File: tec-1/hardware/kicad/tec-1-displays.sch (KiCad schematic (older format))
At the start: 67 parts, among them J2 Conn_01x02, J3 LCD, Q1 2N3904, Q10 AO3400A, Q11 AO3400A, Q12 AO3400A, Q13 AO3400A, Q14 AO3400A, Q15 AO3400A, Q16 AO3400A, Q17 AO3400A, Q18 AO3400A, Q19 AO3400A, Q2 AO3400A, Q20 AO3400A, Q21 AO3400A, Q22 AO3400A, Q23 AO3400A, Q3 AO3400A, Q4 AO3400A, Q5 AO3400A, Q6 AO3400A, Q7 AO3400A, Q8 AO3400A, Q9 AO3400A, U10 74HCT574, U11 74HCT574, U12 LED_SEGMENT_CC_x2, U13 LED_SEGMENT_CC_x4, U14 74HCT574, U15 74HCT574, U16 74HCT574

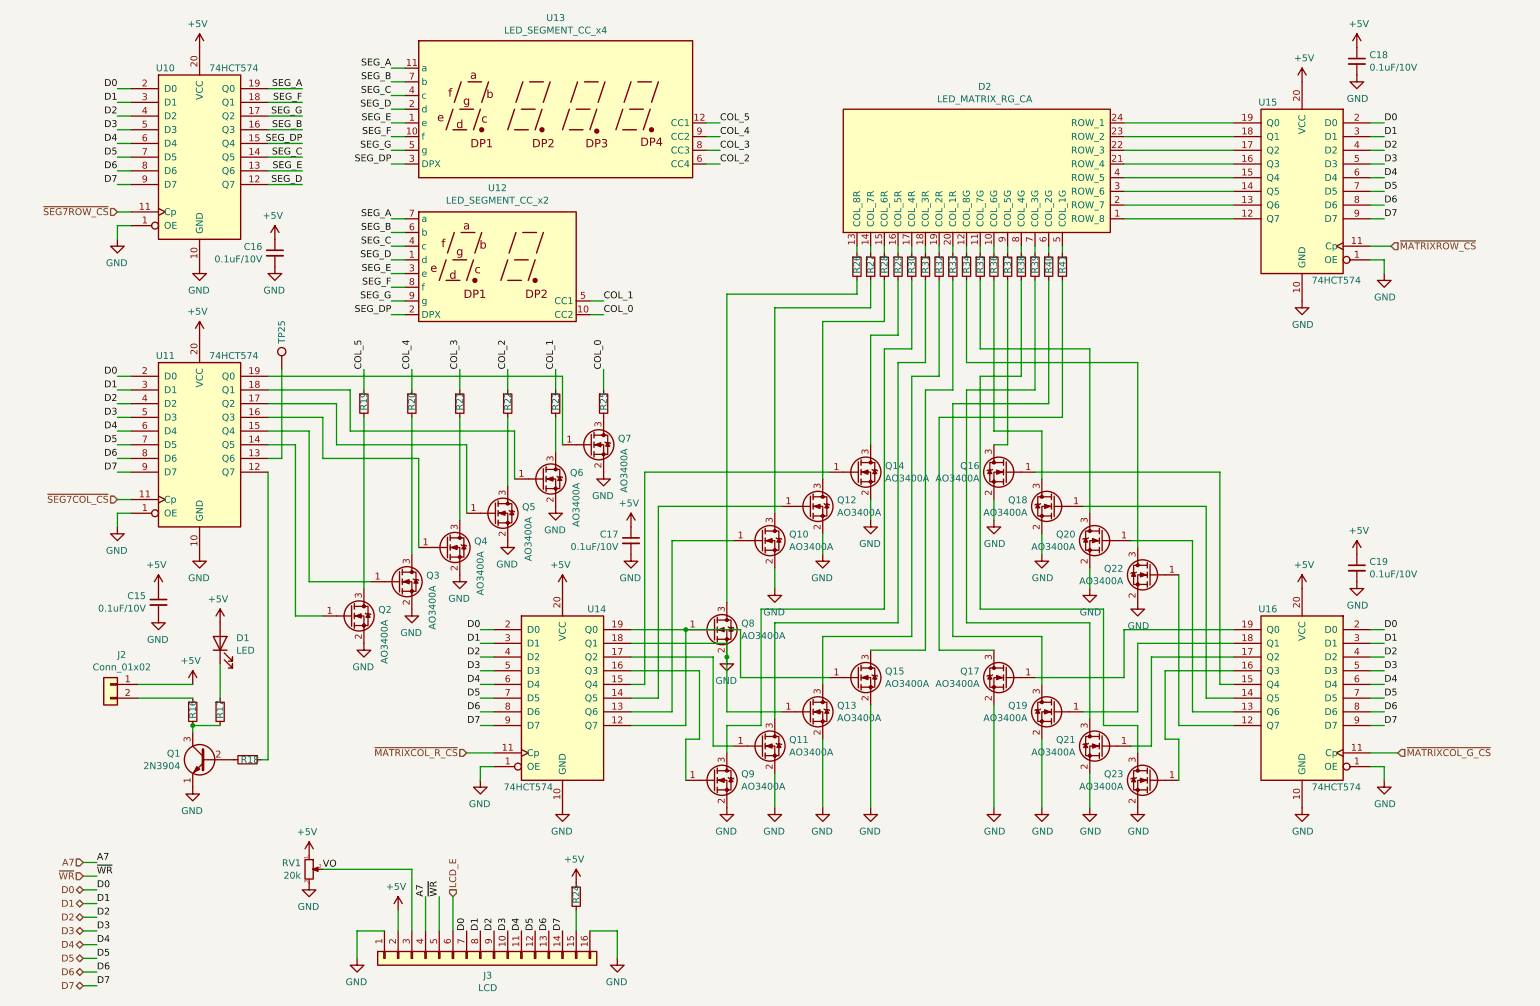
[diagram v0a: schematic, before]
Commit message: tec-1/hardware/kicad: progress checkin - add clock & 207 unrouted
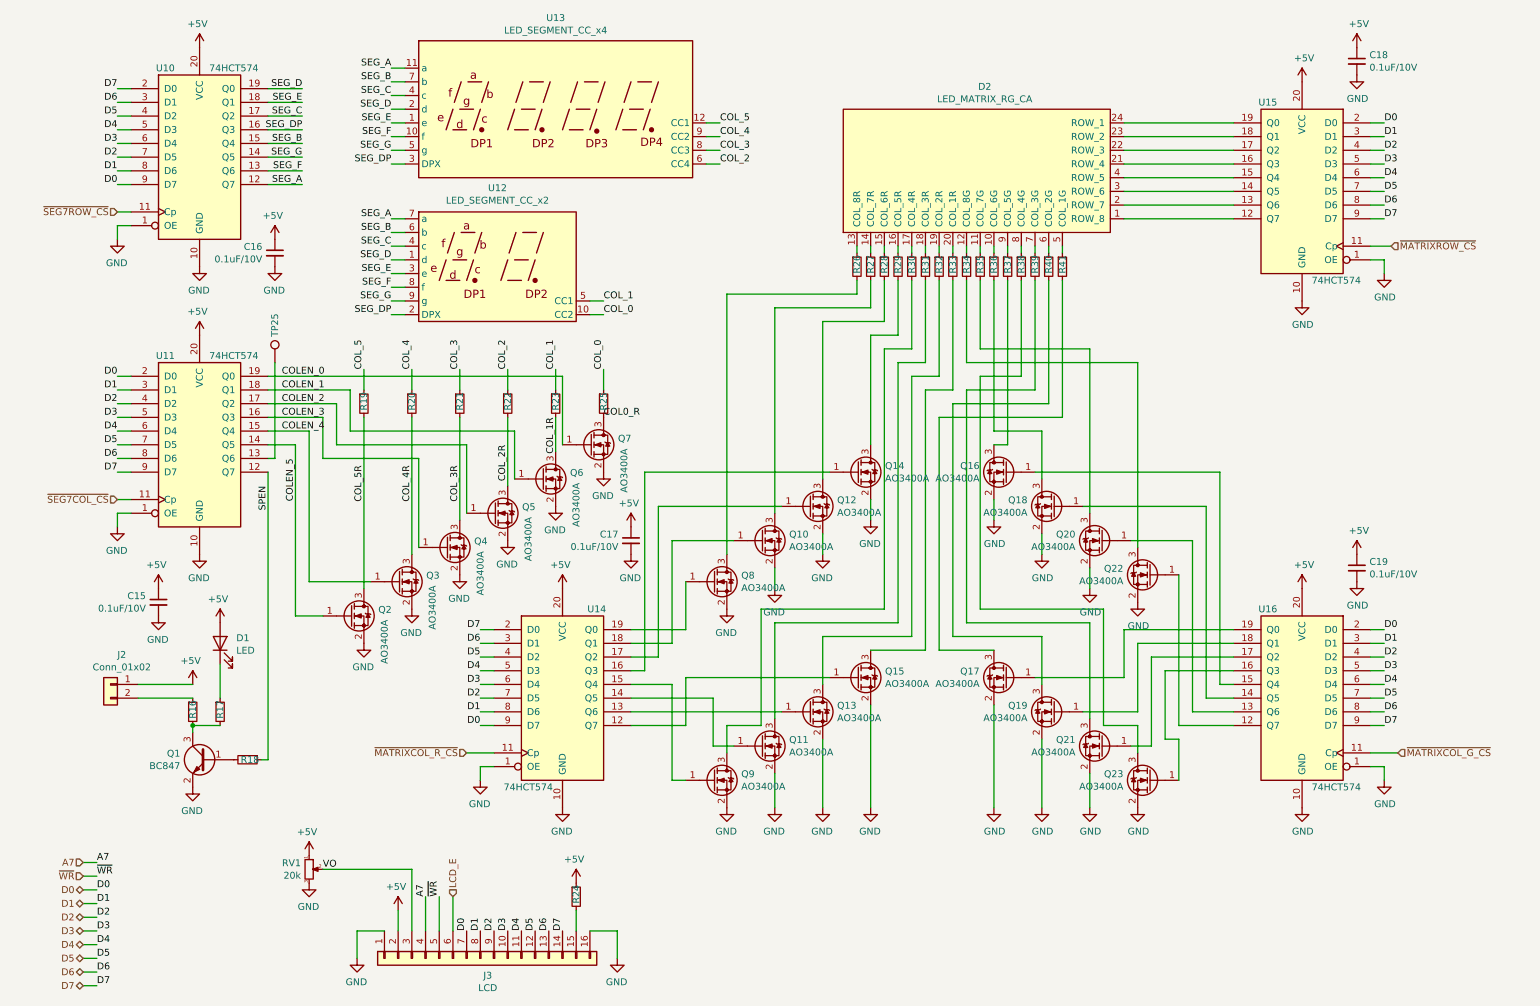
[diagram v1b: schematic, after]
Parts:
- removed Q1: 2N3904, tec-1:TO-92_Inline, symbol tec-1:2N3904
- added Q1: BC847, tec-1:SOT-23, symbol tec-1:BC847
- J2: footprint tec-1:PinHeader_1x02_P2.54mm_Vertical -> tec-1:JST_PH_S2B-PH-SM4-TB_1x02-1MP_P2.00mm_Horizontal
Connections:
- net D0: now also U10.9 (D7), U14.9 (D7); no longer U10.2 (D0), U14.2 (D0)
- net D1: now also U10.8 (D6), U14.8 (D6); no longer U10.3 (D1), U14.3 (D1)
- net D2: now also U10.7 (D5), U14.7 (D5); no longer U10.4 (D2), U14.4 (D2)
- net D3: now also U10.6 (D4), U14.6 (D4); no longer U10.5 (D3), U14.5 (D3)
- net D4: now also U10.5 (D3), U14.5 (D3); no longer U10.6 (D4), U14.6 (D4)
- net D5: now also U10.4 (D2), U14.4 (D2); no longer U10.7 (D5), U14.7 (D5)
- net D6: now also U10.3 (D1), U14.3 (D1); no longer U10.8 (D6), U14.8 (D6)
- net D7: now also U10.2 (D0), U14.2 (D0); no longer U10.9 (D7), U14.9 (D7)
- net GND: now also Q1.2 (E); no longer Q13.1 (G), U14.18 (Q1)
- net SEG_A: now also U10.12 (Q7); no longer U10.19 (Q0)
- net SEG_B: now also U10.15 (Q4); no longer U10.16 (Q3)
- net SEG_C: now also U10.17 (Q2); no longer U10.14 (Q5)
- net SEG_D: now also U10.19 (Q0); no longer U10.12 (Q7)
- net SEG_DP: now also U10.16 (Q3); no longer U10.15 (Q4)
- net SEG_E: now also U10.18 (Q1); no longer U10.13 (Q6)
- net SEG_F: now also U10.13 (Q6); no longer U10.18 (Q1)
- net SEG_G: now also U10.14 (Q5); no longer U10.17 (Q2)
- net at Q15.1 (G), U14.12 (Q7): no longer Q8.1 (G), U14.19 (Q0)
- net at U14.13 (Q6): now also Q13.1 (G); no longer Q10.1 (G)
- net at U14.14 (Q5): now also Q11.1 (G); no longer Q12.1 (G)
- net at U14.15 (Q4): now also Q9.1 (G); no longer Q14.1 (G)
- net at U14.16 (Q3): now also Q14.1 (G); no longer Q9.1 (G)
- net at U14.17 (Q2): now also Q12.1 (G); no longer Q11.1 (G)
- net SPEN: now reaches R18.1, U11.12 (Q7)
- net COLEN_5: now reaches Q2.1 (G), U11.14 (Q5)
- net COLEN_4: now reaches Q3.1 (G), U11.15 (Q4)
- net COLEN_3: now reaches Q4.1 (G), U11.16 (Q3)
- net COLEN_2: now reaches Q5.1 (G), U11.17 (Q2)
- net COLEN_1: now reaches Q6.1 (G), U11.18 (Q1)
- net COLEN_0: now reaches Q7.1 (G), U11.19 (Q0)
- net COL_3R: now reaches Q4.3 (D), R21.2
- net COL_4R: now reaches Q3.3 (D), R20.2
- net COL_5R: now reaches Q2.3 (D), R19.2
- net COL0_R: now reaches Q7.3 (D), R25.2
- net COL_1R: now reaches Q6.3 (D), R23.2
- net COL_2R: now reaches Q5.3 (D), R22.2
- net at R18.2: now also Q1.1 (B)
- net at R16.2, R17.2: now also Q1.3 (C)
- new net: Q10.1 (G), U14.18 (Q1)
- new net: Q8.1 (G), U14.19 (Q0)
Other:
- moved on the sheet: Q8, TP25

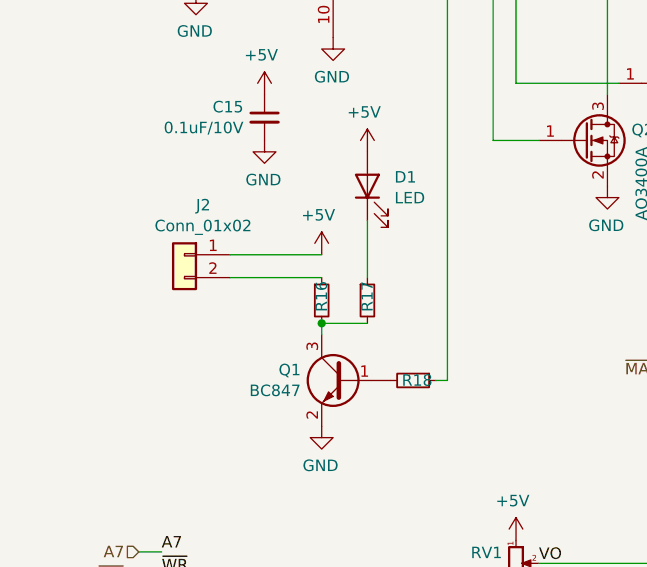
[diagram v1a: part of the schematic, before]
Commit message: tec-1/hardware/kicad: routing complete, all DRC errors checked as ok
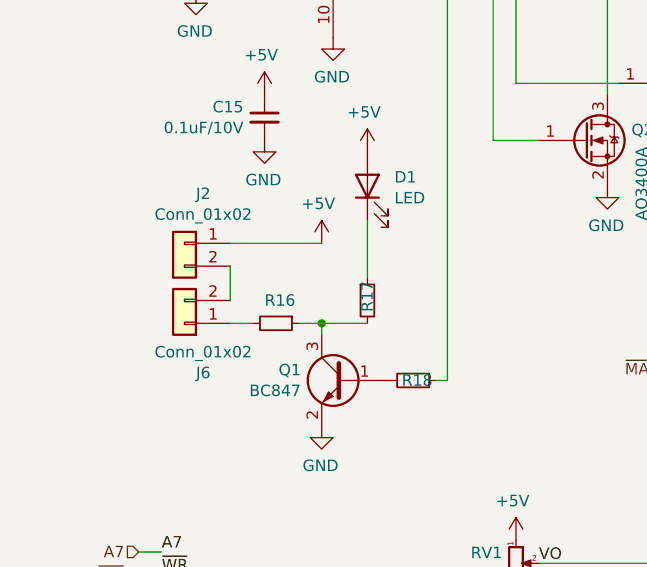
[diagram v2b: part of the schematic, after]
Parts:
- added J6: Conn_01x02, tec-1:PinHeader_1x02_P2.54mm_Vertical, symbol tec-1:Conn_01x02
- RV1: footprint (none) -> tec-1:Potentiometer_Bourns_TC33X_Vertical
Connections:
- net at J2.2 (Pin_2): now also J6.2 (Pin_2); no longer R16.1
- net at Q1.3 (C), R17.2: now also R16.1; no longer R16.2
- new net: J6.1 (Pin_1), R16.2
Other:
- moved on the sheet: J2, R16
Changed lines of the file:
@@
 L tec-1:R R16
 U 1 1 61302CC9
-P 1600 5600
-F 0 "R16" V 1600 5550 50  0000 L CNN
-F 1 "100R" H 1659 5555 50  0001 L CNN
-F 2 "tec-1:R_0805_2012Metric" H 1600 5600 50  0001 C CNN
-F 3 "~" H 1600 5600 50  0001 C CNN
-	1    1600 5600
-	1    0    0    -1
+P 1400 5700
+F 0 "R16" V 1300 5650 50  0000 L CNN
+F 1 "100R" H 1459 5655 50  0001 L CNN
+F 2 "tec-1:R_0805_2012Metric" H 1400 5700 50  0001 C CNN
+F 3 "~" H 1400 5700 50  0001 C CNN
+	1    1400 5700
+	0    1    1    0
 $EndComp
 $Comp
 L tec-1:Conn_01x02 J2
 U 1 1 61351741
-P 1000 5400
-F 0 "J2" H 918 5617 50  0000 C CNN
-F 1 "Conn_01x02" H 918 5526 50  0000 C CNN
-F 2 "tec-1:JST_PH_S2B-PH-SM4-TB_1x02-1MP_P2.00mm_Horizontal" H 1000 5400 50  0001 C CNN
-F 3 "~" H 1000 5400 50  0001 C CNN
-	1    1000 5400
+P 1000 5350
+F 0 "J2" H 918 5567 50  0000 C CNN
+F 1 "Conn_01x02" H 918 5476 50  0000 C CNN
+F 2 "tec-1:JST_PH_S2B-PH-SM4-TB_1x02-1MP_P2.00mm_Horizontal" H 1000 5350 50  0001 C CNN
+F 3 "~" H 1000 5350 50  0001 C CNN
+	1    1000 5350
 	-1   0    0    -1
 $EndComp
@@
 L power:+5V #PWR065
 U 1 1 6135291F
-P 1600 5400
-F 0 "#PWR065" H 1600 5250 50  0001 C CNN
-F 1 "+5V" H 1615 5573 50  0000 C CNN
-F 2 "" H 1600 5400 50  0001 C CNN
-F 3 "" H 1600 5400 50  0001 C CNN
-	1    1600 5400
+P 1600 5350
+F 0 "#PWR065" H 1600 5200 50  0001 C CNN
+F 1 "+5V" H 1615 5523 50  0000 C CNN
+F 2 "" H 1600 5350 50  0001 C CNN
+F 3 "" H 1600 5350 50  0001 C CNN
+	1    1600 5350
 	-1   0    0    -1
 $EndComp
 Wire Wire Line
-	1200 5400 1600 5400
+	1200 5350 1600 5350
 Wire Wire Line
 	1600 5700 1600 5750
@@
 	0    -1   -1   0
 $EndComp
-Wire Wire Line
-	1600 5500 1200 5500
 $Comp
 L tec-1:R R17
@@
 Wire Wire Line
 	1600 5700 1800 5700
-Connection ~ 1600 5700
 $Comp
 L tec-1:R R19
@@
 F 0 "RV1" H 2390 6796 50  0000 R CNN
 F 1 "20k" H 2390 6705 50  0000 R CNN
-F 2 "" H 2450 6750 50  0001 C CNN
+F 2 "tec-1:Potentiometer_Bourns_TC33X_Vertical" H 2450 6750 50  0001 C CNN
 F 3 "~" H 2450 6750 50  0001 C CNN
 	1    2450 6750
@@
 Wire Wire Line
 	4900 5300 4900 3850
+$Comp
+L tec-1:Conn_01x02 J6
+U 1 1 60883CC6
+P 1000 5700
+F 0 "J6" H 918 5917 50  0000 C CNN
+F 1 "Conn_01x02" H 918 5826 50  0000 C CNN
+F 2 "tec-1:PinHeader_1x02_P2.54mm_Vertical" H 1000 5700 50  0001 C CNN
+F 3 "~" H 1000 5700 50  0001 C CNN
+	1    1000 5700
+	-1   0    0    1
+$EndComp
+Wire Wire Line
+	1200 5450 1200 5600
+Wire Wire Line
+	1600 5700 1500 5700
+Connection ~ 1600 5700
+Wire Wire Line
+	1300 5700 1200 5700
 $EndSCHEMATC
